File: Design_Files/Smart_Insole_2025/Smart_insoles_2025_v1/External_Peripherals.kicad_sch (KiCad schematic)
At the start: 9 parts, among them U2 CD74HC4067M96, U3 LSM6DSO32TR

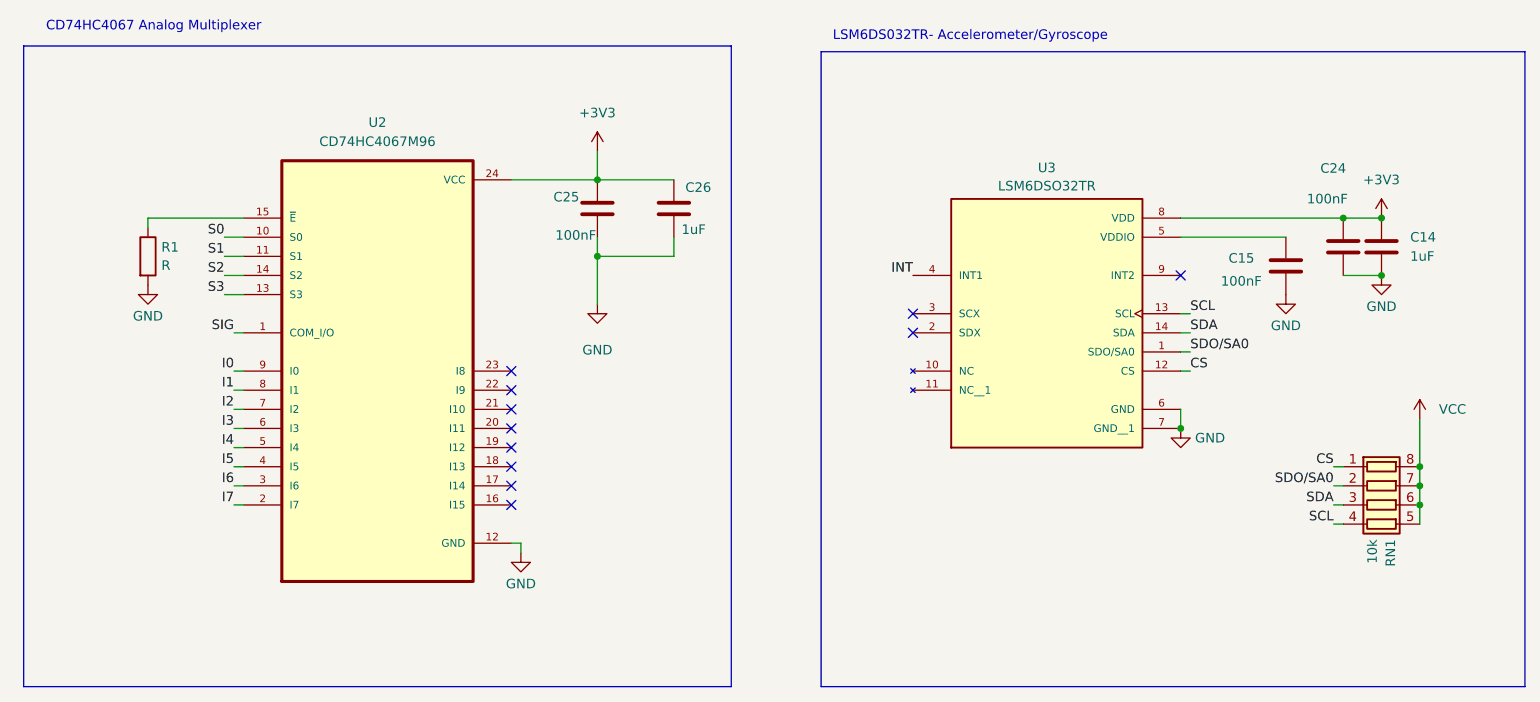
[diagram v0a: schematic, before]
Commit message: SCH:Solved Errors in ERC
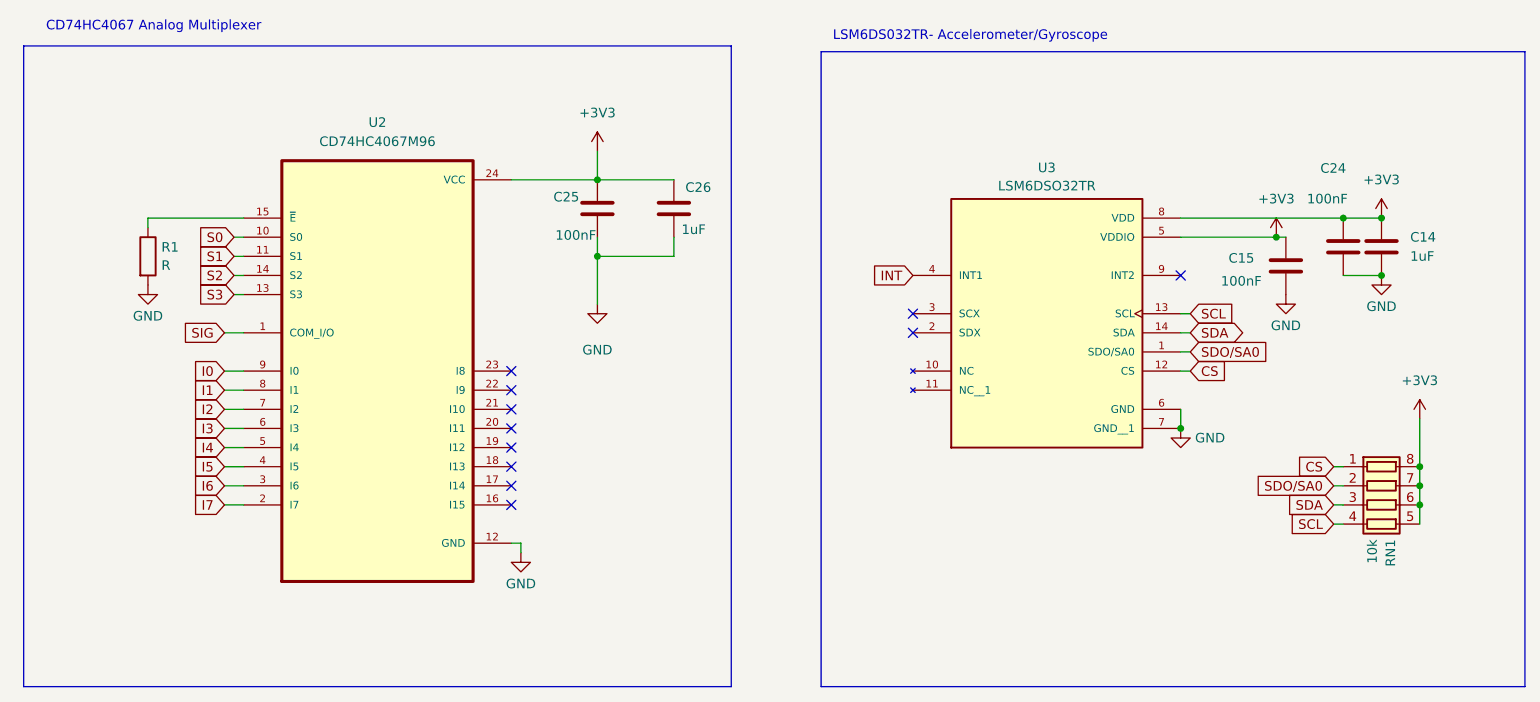
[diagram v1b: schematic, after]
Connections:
- net VCC is gone; now on net +3V3: RN1.5 (R4.2), RN1.6 (R3.2), RN1.7 (R2.2), RN1.8 (R1.2)
- net +3V3: now also C15.1, U3.5 (VDDIO)
- net SDO/SA0 renamed SDO/SA0

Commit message: SCH: Added missing footprints. PCB: Grouped related components for new layout
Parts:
- C14, C15, C24, C25, C26: footprint Capacitor_SMD:C_0603_1608Metric_Pad1.08x0.95mm_HandSolder -> Capacitor_SMD:C_0805_2012Metric_Pad1.18x1.45mm_HandSolder
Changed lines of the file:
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@@
 			)
 		)
-		(property "Footprint" "Capacitor_SMD:C_0603_1608Metric_Pad1.08x0.95mm_HandSolder"
+		(property "Footprint" "Capacitor_SMD:C_0805_2012Metric_Pad1.18x1.45mm_HandSolder"
 			(at 97.4852 48.26 0)
 			(effects
@@
 			)
 		)
-		(property "Footprint" "Capacitor_SMD:C_0603_1608Metric_Pad1.08x0.95mm_HandSolder"
+		(property "Footprint" "Capacitor_SMD:C_0805_2012Metric_Pad1.18x1.45mm_HandSolder"
 			(at 107.6452 48.26 0)
 			(effects
@@
 			)
 		)
-		(property "Footprint" "Capacitor_SMD:C_0603_1608Metric_Pad1.08x0.95mm_HandSolder"
+		(property "Footprint" "Capacitor_SMD:C_0805_2012Metric_Pad1.18x1.45mm_HandSolder"
 			(at 188.9252 55.88 0)
 			(effects
@@
 			)
 		)
-		(property "Footprint" "Capacitor_SMD:C_0603_1608Metric_Pad1.08x0.95mm_HandSolder"
+		(property "Footprint" "Capacitor_SMD:C_0805_2012Metric_Pad1.18x1.45mm_HandSolder"
 			(at 201.6252 53.34 0)
 			(effects
@@
 			)
 		)
-		(property "Footprint" "Capacitor_SMD:C_0603_1608Metric_Pad1.08x0.95mm_HandSolder"
+		(property "Footprint" "Capacitor_SMD:C_0805_2012Metric_Pad1.18x1.45mm_HandSolder"
 			(at 196.5452 53.34 0)
 			(effects

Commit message: SCH: Fixed Warnings. Added thermistor solder pads library.
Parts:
- R1: footprint Resistor_SMD:R_0603_1608Metric_Pad0.98x0.95mm_HandSolder -> Resistor_SMD:R_0805_2012Metric
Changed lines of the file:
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@@
 			)
 		)
-		(property "Footprint" "Resistor_SMD:R_0603_1608Metric_Pad0.98x0.95mm_HandSolder"
+		(property "Footprint" "Resistor_SMD:R_0805_2012Metric"
 			(at 35.052 50.8 90)
 			(effects
@@
 			(at 36.83 50.8 0)
 			(effects
+				(font
+					(size 1.27 1.27)
+				)
+				(hide yes)
+			)
+		)
+		(property "MPN" ""
+			(at 36.83 50.8 0)
+			(effects
+				(font
+					(size 1.27 1.27)
+				)
+				(hide yes)
+			)
+		)
+		(property "Manufacturer" ""
+			(at 36.83 50.8 0)
+			(effects
+				(font
+					(size 1.27 1.27)
+				)
+				(hide yes)
+			)
+		)
+		(property "3D Model" ""
+			(at 36.83 50.8 0)
+			(effects
+				(font
+					(size 1.27 1.27)
+				)
+				(hide yes)
+			)
+		)
+		(property "Notes" ""
+			(at 36.83 50.8 0)
+			(effects
+				(font
+					(size 1.27 1.27)
+				)
+				(hide yes)
+			)
+		)
+		(property "LCSC Part #" ""
+			(at 36.83 50.8 0)
+			(effects
+				(font
+					(size 1.27 1.27)
+				)
+				(hide yes)
+			)
+		)
+		(property "LCSC MPN" ""
+			(at 36.83 50.8 0)
+			(effects
+				(font
+					(size 1.27 1.27)
+				)
+				(hide yes)
+			)
+		)
+		(property "LCSC MANUFACTURER" ""
+			(at 36.83 50.8 0)
+			(effects

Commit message: SCH: Added test points on idle MCU pins and Power supply. Added ON/OFF switch on VSEL.
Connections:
- net SDX: now reaches U3.2 (SDX)
- net SCX: now reaches U3.3 (SCX)
- net INT2: now reaches U3.9 (INT2)
- no-connect marks 11 -> 8
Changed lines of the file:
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@@
-	)
-	(no_connect
-		(at 138.43 60.96)
-	)
-	(no_connect
-		(at 138.43 58.42)
 	)
 	(no_connect
@@
 	)
 	(no_connect
-		(at 173.99 53.34)
-	)
-	(no_connect
 		(at 85.09 71.12)
 	)
@@
 		)
 	)
+	(global_label "INT2"
+		(shape output)
+		(at 173.99 53.34 0)
+		(effects
+			(font
+				(size 1.27 1.27)
+			)
+			(justify left)
+		)
+		(property "Intersheetrefs" "${INTERSHEET_REFS}"
+			(at 173.99 53.34 0)
+			(effects
+				(font
+					(size 1.27 1.27)
+				)
+				(hide yes)
+			)
+		)
+	)
 	(global_label "I2"
 		(shape input)
@@
 				)
 				(justify right)
+				(hide yes)
+			)
+		)
+	)
+	(global_label "SDX"
+		(shape input)
+		(at 138.43 60.96 180)
+		(effects
+			(font
+				(size 1.27 1.27)
+			)
+			(justify right)
+		)
+		(property "Intersheetrefs" "${INTERSHEET_REFS}"
+			(at 138.43 60.96 0)
+			(effects
+				(font
+					(size 1.27 1.27)
+				)
 				(hide yes)
 			)
@@
 				)
 				(justify left)
+				(hide yes)
+			)
+		)
+	)
+	(global_label "SCX"
+		(shape input)
+		(at 138.43 58.42 180)
+		(effects
+			(font
+				(size 1.27 1.27)
+			)
+			(justify right)
+		)
+		(property "Intersheetrefs" "${INTERSHEET_REFS}"
+			(at 138.43 58.42 0)
+			(effects
+				(font
+					(size 1.27 1.27)
+				)
 				(hide yes)
 			)
@@
 		(dnp no)
 		(property "Reference" "C15"
-			(at 180.34 51.054 0)
+			(at 182.88 50.038 0)
 			(effects
 				(font
@@
 		)
 		(property "Value" "100nF"
-			(at 179.324 54.102 0)
-			(effects
-				(font
+			(at 181.864 54.356 0)
+			(effects
+				(font

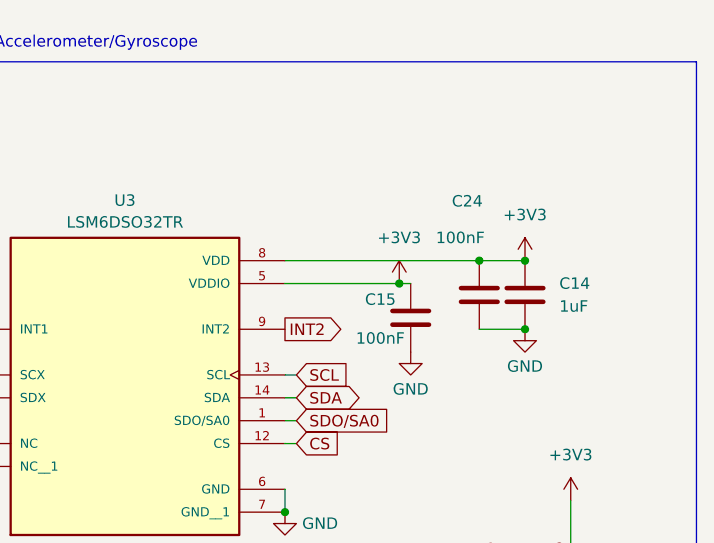
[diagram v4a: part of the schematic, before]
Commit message: PCB:USB Differential pair Impedance calculation and Routing. Also Organized Silkscreen. Added text polarity to battery, boot and rst buttons, and RX TX
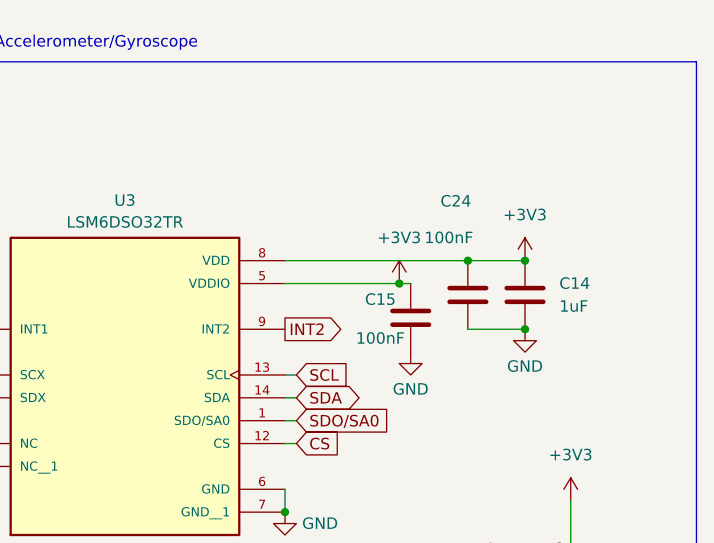
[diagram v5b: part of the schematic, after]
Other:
- moved on the sheet: C24
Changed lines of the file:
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@@
 	)
 	(junction
-		(at 195.58 45.72)
+		(at 194.31 45.72)
 		(diameter 0)
 		(color 0 0 0 0)
@@
 	(wire
 		(pts
-			(xy 195.58 45.72) (xy 173.99 45.72)
+			(xy 194.31 45.72) (xy 200.66 45.72)
 		)
 		(stroke
@@
 	(wire
 		(pts
+			(xy 194.31 45.72) (xy 173.99 45.72)
+		)
+		(stroke
+			(width 0)
+			(type default)
+		)
+	)
+	(wire
+		(pts
 			(xy 195.58 83.82) (xy 194.31 83.82)
 		)
@@
 	(wire
 		(pts
-			(xy 200.66 45.72) (xy 195.58 45.72)
-		)
-		(stroke
-			(width 0)
-			(type default)
-		)
-	)
-	(wire
-		(pts
 			(xy 46.99 78.74) (xy 49.53 78.74)
 		)
@@
 	(wire
 		(pts
-			(xy 195.58 53.34) (xy 200.66 53.34)
+			(xy 194.31 53.34) (xy 200.66 53.34)
 		)
 		(stroke
@@
 	(symbol
 		(lib_id "Device:C")
-		(at 195.58 49.53 0)
+		(at 194.31 49.53 0)
 		(unit 1)
 		(exclude_from_sim no)
@@
 		(dnp no)
 		(property "Reference" "C24"
-			(at 192.532 39.116 0)
+			(at 191.262 39.116 0)
 			(effects
 				(font
@@
 		)
 		(property "Value" "100nF"
-			(at 190.754 43.18 0)
+			(at 189.484 43.18 0)
 			(effects
 				(font
@@
 		)
 		(property "Footprint" "Capacitor_SMD:C_0805_2012Metric_Pad1.18x1.45mm_HandSolder"
-			(at 196.5452 53.34 0)
+			(at 195.2752 53.34 0)
 			(effects
 				(font
@@
 		)
 		(property "Datasheet" "~"
-			(at 195.58 49.53 0)
+			(at 194.31 49.53 0)
 			(effects
 				(font
@@
 		)
 		(property "Description" "Unpolarized capacitor"
-			(at 195.58 49.53 0)
-			(effects
-				(font
+			(at 194.31 49.53 0)
+			(effects
+				(font

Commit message: PCB:Fixed Multiplexer wrong footprint. Flex Connector modified. Fixed DRC Errors and Warnings
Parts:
- U2: footprint CD74HC4067:SOIC127P1030X265-24N -> Package_SO:TSSOP-24_4.4x7.8mm_P0.65mm
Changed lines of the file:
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@@
 			)
 		)
-		(property "Footprint" "CD74HC4067:SOIC127P1030X265-24N"
+		(property "Footprint" "Package_SO:TSSOP-24_4.4x7.8mm_P0.65mm"
 			(at 67.31 66.04 0)
 			(effects
@@
 				)
 				(justify bottom)
+				(hide yes)
+			)
+		)
+		(property "MPN" ""
+			(at 67.31 66.04 0)
+			(effects
+				(font
+					(size 1.27 1.27)
+				)
+				(hide yes)
+			)
+		)
+		(property "Manufacturer" ""
+			(at 67.31 66.04 0)
+			(effects
+				(font
+					(size 1.27 1.27)
+				)
+				(hide yes)
+			)
+		)
+		(property "3D Model" ""
+			(at 67.31 66.04 0)
+			(effects
+				(font
+					(size 1.27 1.27)
+				)
+				(hide yes)
+			)
+		)
+		(property "Notes" ""
+			(at 67.31 66.04 0)
+			(effects
+				(font
+					(size 1.27 1.27)
+				)
+				(hide yes)
+			)
+		)
+		(property "LCSC Part #" ""
+			(at 67.31 66.04 0)
+			(effects
+				(font
+					(size 1.27 1.27)
+				)
+				(hide yes)
+			)
+		)
+		(property "LCSC MPN" ""
+			(at 67.31 66.04 0)
+			(effects
+				(font
+					(size 1.27 1.27)
+				)
+				(hide yes)
+			)
+		)
+		(property "LCSC MANUFACTURER" ""
+			(at 67.31 66.04 0)
+			(effects
+				(font
+					(size 1.27 1.27)
+				)
 				(hide yes)
 			)
@@
 				(hide yes)
 			)
+		)
+		(property "MPN" ""
+			(at 156.21 58.42 0)
+			(effects
+				(font
+					(size 1.27 1.27)
+				)
+				(hide yes)
+			)
+		)
+		(property "Manufacturer" ""
+			(at 156.21 58.42 0)
+			(effects
+				(font
+					(size 1.27 1.27)
+				)
+				(hide yes)
+			)
+		)
+		(property "3D Model" ""
+			(at 156.21 58.42 0)
+			(effects
+				(font
+					(size 1.27 1.27)
+				)
+				(hide yes)
+			)
+		)
+		(property "Notes" ""
+			(at 156.21 58.42 0)
+			(effects
+				(font
+					(size 1.27 1.27)
+				)
+				(hide yes)
+			)
+		)
+		(property "LCSC Part #" ""
+			(at 156.21 58.42 0)
+			(effects
+				(font
+					(size 1.27 1.27)
+				)
+				(hide yes)
+			)
+		)
+		(property "LCSC MPN" ""
+			(at 156.21 58.42 0)
+			(effects
+				(font
+					(size 1.27 1.27)
+				)
+				(hide yes)
+			)
+		)
+		(property "LCSC MANUFACTURER" ""
+			(at 156.21 58.42 0)
+			(effects
+				(font
+					(size 1.27 1.27)
+				)
+				(hide yes)
+			)

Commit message: Modified some footprints to better fit real components.
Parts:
- U2: footprint Package_SO:TSSOP-24_4.4x7.8mm_P0.65mm -> Package_SO:TSSOP-24_6.1x7.8mm_P0.65mm
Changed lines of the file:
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@@
 			)
 		)
-		(property "Footprint" "Package_SO:TSSOP-24_4.4x7.8mm_P0.65mm"
+		(property "Footprint" "Package_SO:TSSOP-24_6.1x7.8mm_P0.65mm"
 			(at 67.31 66.04 0)
 			(effects
